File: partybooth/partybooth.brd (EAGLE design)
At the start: 59.7 x 39 mm, 21 parts, among them IC1 TINY13-20PU, IC2 78L05Z, J1 Lamp, J2 Button, J3 12V, T1 2N3904, T2 2N3904, X1 1501_06

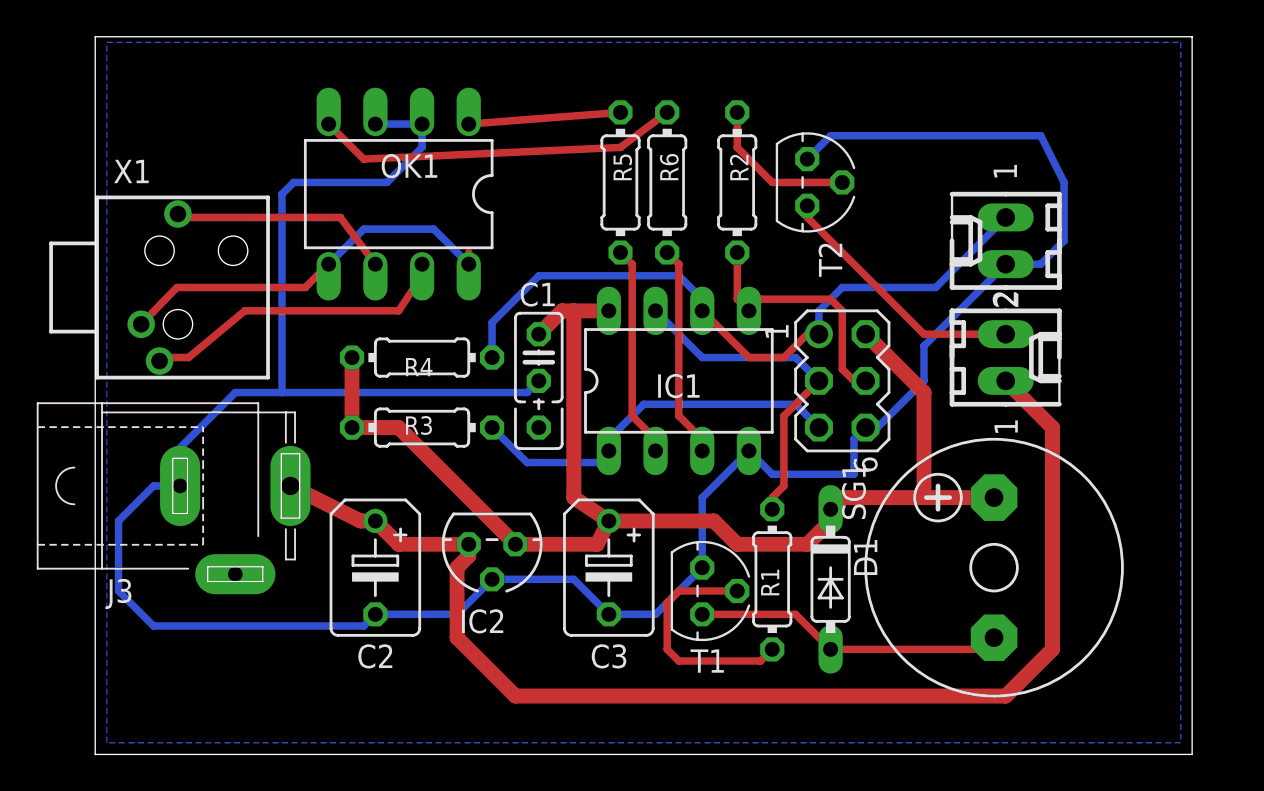
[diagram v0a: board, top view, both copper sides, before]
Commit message: 
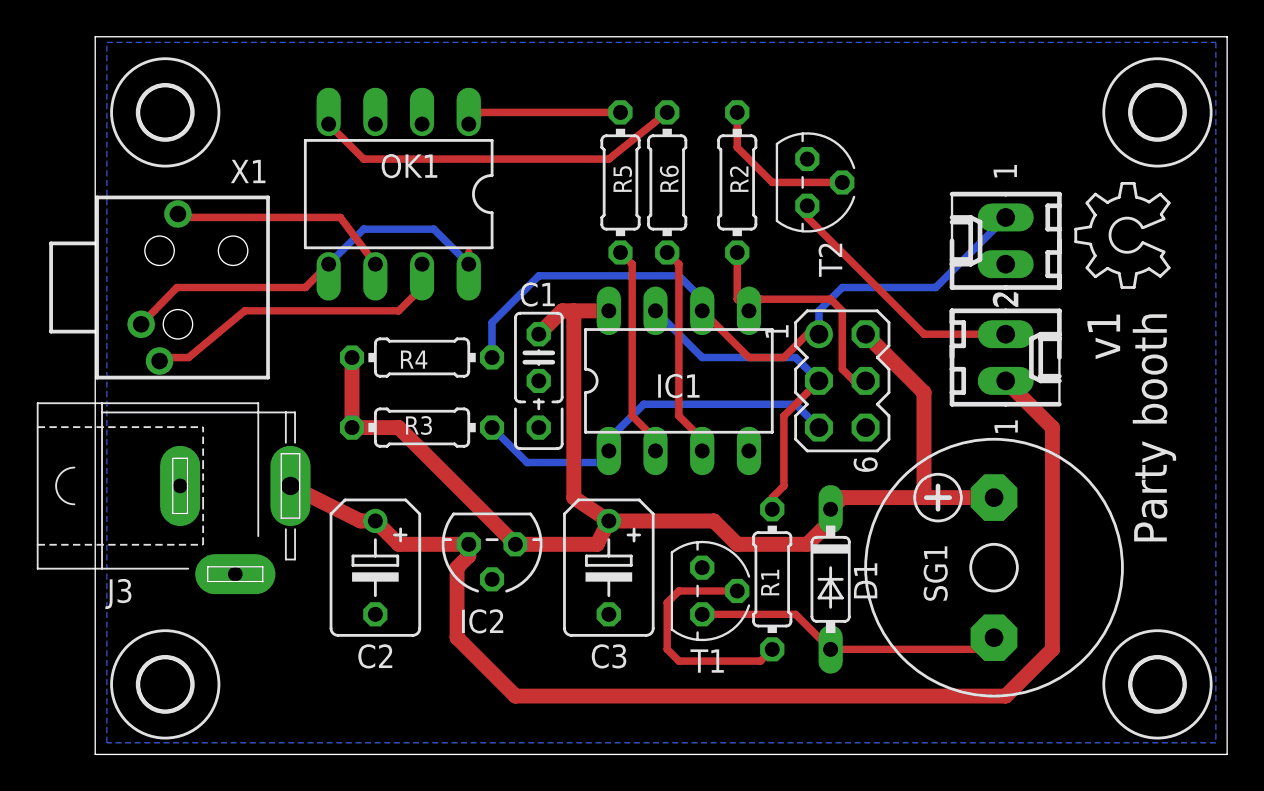
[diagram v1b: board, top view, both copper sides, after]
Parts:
- added U$1: (no value), ohw-logo:OSHW_6X200_NOTEXT
- added U$2, U$3, U$4, U$5: (no value), holes:2,8
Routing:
- net GND: track 141.7 -> 0.00 mm
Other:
- board size 59.7 x 39 mm -> 61.6 x 39 mm
- board text added: "Party booth"
- board text added: "v1"

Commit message: 
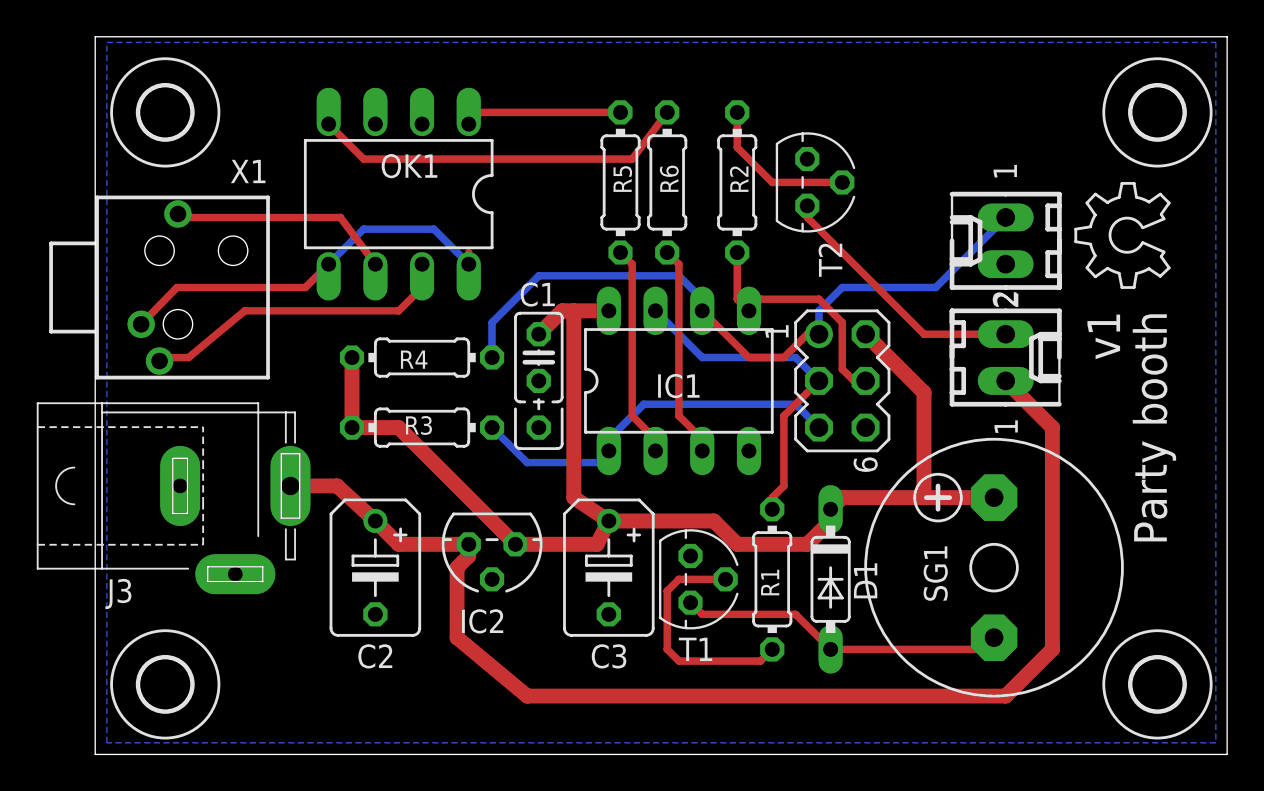
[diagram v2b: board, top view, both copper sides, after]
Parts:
- moved T1 0.90 mm to (32.4, 9.53)
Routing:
- net N$2: track 16.9 -> 17.8 mm
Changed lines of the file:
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@@
 <layer number="21" name="tPlace" color="7" fill="1" visible="yes" active="yes"/>
 <layer number="22" name="bPlace" color="7" fill="1" visible="yes" active="yes"/>
-<layer number="23" name="tOrigins" color="15" fill="1" visible="no" active="yes"/>
+<layer number="23" name="tOrigins" color="15" fill="1" visible="yes" active="yes"/>
 <layer number="24" name="bOrigins" color="15" fill="1" visible="no" active="yes"/>
 <layer number="25" name="tNames" color="7" fill="1" visible="yes" active="yes"/>
@@
 <attribute name="VALUE" x="52.705" y="5.715" size="1.27" layer="27" ratio="10" rot="R90"/>
 </element>
-<element name="T1" library="transistor" package="TO92" value="2N3904" x="33.02" y="8.89" smashed="yes" rot="R270">
-<attribute name="NAME" x="32.385" y="4.445" size="1.27" layer="25" ratio="10"/>
+<element name="T1" library="transistor" package="TO92" value="2N3904" x="32.385" y="9.525" smashed="yes" rot="R270">
+<attribute name="NAME" x="31.75" y="5.08" size="1.27" layer="25" ratio="10"/>
 </element>
 <element name="T2" library="transistor" package="TO92" value="2N3904" x="38.735" y="31.115" smashed="yes" rot="R270">
@@
 <contactref element="T1" pad="2"/>
 <contactref element="R1" pad="2"/>
-<wire x1="34.925" y1="8.89" x2="31.75" y2="8.89" width="0.4064" layer="1"/>
-<wire x1="31.75" y1="8.89" x2="31.115" y2="8.255" width="0.4064" layer="1"/>
-<wire x1="31.115" y1="8.255" x2="31.115" y2="5.715" width="0.4064" layer="1"/>
+<wire x1="34.29" y1="9.525" x2="31.75" y2="9.525" width="0.4064" layer="1"/>
+<wire x1="31.75" y1="9.525" x2="31.115" y2="8.89" width="0.4064" layer="1"/>
+<wire x1="31.115" y1="8.89" x2="31.115" y2="5.715" width="0.4064" layer="1"/>
 <wire x1="31.115" y1="5.715" x2="31.75" y2="5.08" width="0.4064" layer="1"/>
 <wire x1="31.75" y1="5.08" x2="36.195" y2="5.08" width="0.4064" layer="1"/>
@@
 <contactref element="SG1" pad="-"/>
 <contactref element="T1" pad="1"/>
+<wire x1="32.385" y1="8.255" x2="33.02" y2="7.62" width="0.4064" layer="1"/>
 <wire x1="33.02" y1="7.62" x2="38.1" y2="7.62" width="0.4064" layer="1"/>
 <wire x1="38.1" y1="7.62" x2="40.005" y2="5.715" width="0.4064" layer="1"/>
@@
 <contactref element="IC2" pad="3"/>
 <contactref element="J3" pad="3"/>
-<wire x1="10.62" y1="14.605" x2="14.43" y2="12.7" width="0.8128" layer="1"/>
-<wire x1="14.43" y1="12.7" x2="15.24" y2="12.7" width="0.8128" layer="1"/>
+<wire x1="10.62" y1="14.605" x2="13.16" y2="14.605" width="0.8128" layer="1"/>
+<wire x1="13.16" y1="14.605" x2="15.24" y2="12.7" width="0.8128" layer="1"/>
 <wire x1="15.24" y1="12.7" x2="16.51" y2="11.43" width="0.8128" layer="1"/>
 <wire x1="16.51" y1="11.43" x2="20.32" y2="11.43" width="0.8128" layer="1"/>
@@
 <wire x1="52.07" y1="17.78" x2="52.07" y2="5.715" width="0.8128" layer="1"/>
 <wire x1="52.07" y1="5.715" x2="49.53" y2="3.175" width="0.8128" layer="1"/>
-<wire x1="49.53" y1="3.175" x2="22.86" y2="3.175" width="0.8128" layer="1"/>
-<wire x1="22.86" y1="3.175" x2="19.685" y2="6.35" width="0.8128" layer="1"/>
+<wire x1="49.53" y1="3.175" x2="23.495" y2="3.175" width="0.8128" layer="1"/>
+<wire x1="23.495" y1="3.175" x2="19.685" y2="6.35" width="0.8128" layer="1"/>
 <wire x1="19.685" y1="6.35" x2="19.685" y2="10.16" width="0.8128" layer="1"/>
 <wire x1="19.685" y1="10.16" x2="20.32" y2="10.795" width="0.8128" layer="1"/>
@@
 <wire x1="34.925" y1="24.765" x2="34.925" y2="27.305" width="0.4064" layer="1"/>
 <wire x1="35.56" y1="24.13" x2="36.195" y2="24.765" width="0.4064" layer="1"/>
-<wire x1="36.195" y1="24.765" x2="40.005" y2="24.765" width="0.4064" layer="1"/>
-<wire x1="40.005" y1="24.765" x2="40.64" y2="24.13" width="0.4064" layer="1"/>
-<wire x1="40.64" y1="24.13" x2="40.64" y2="20.955" width="0.4064" layer="1"/>
+<wire x1="36.195" y1="24.765" x2="39.37" y2="24.765" width="0.4064" layer="1"/>
+<wire x1="39.37" y1="24.765" x2="40.64" y2="23.495" width="0.4064" layer="1"/>
+<wire x1="40.64" y1="23.495" x2="40.64" y2="20.955" width="0.4064" layer="1"/>
 <wire x1="40.64" y1="20.955" x2="41.275" y2="20.32" width="0.4064" layer="1"/>
 <wire x1="41.275" y1="20.32" x2="41.91" y2="20.32" width="0.4064" layer="1"/>
@@
 <contactref element="OK1" pad="4"/>
 <contactref element="R6" pad="2"/>
-<wire x1="31.115" y1="34.925" x2="27.94" y2="32.385" width="0.4064" layer="1"/>
-<wire x1="27.94" y1="32.385" x2="14.605" y2="32.385" width="0.4064" layer="1"/>
+<wire x1="31.115" y1="34.925" x2="29.21" y2="32.385" width="0.4064" layer="1"/>
+<wire x1="29.21" y1="32.385" x2="14.605" y2="32.385" width="0.4064" layer="1"/>
 <wire x1="14.605" y1="32.385" x2="12.7" y2="34.29" width="0.4064" layer="1"/>
 </signal>
